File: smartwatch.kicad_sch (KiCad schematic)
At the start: 48 parts, among them IC1 LTC4413EDD-1#PBF, IC2 MIA-M10Q-00B, J3 5022441530, J5 Conn_01x04_Socket, U1 NRF52832-QFAA-R, U10 AP2127K-1.8, U2 AP2112K-3.3TRG1, U3 MAX30102, U6 ESP-PSRAM64, U7 MCP73831-2-OT, U8 W25Q128JVS, U9 LIS2DE12, X1 CX2016DB32000D0WZRC1, X2 9HT10-32.768KBZC-T

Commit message: pcb layout almost complete
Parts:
- removed C10: C, Capacitor_SMD:C_0402_1005Metric, symbol Device:C
- C9: value C -> 0.8pF
- L1: value L -> 3.9nH; footprint Inductor_SMD:L_0603_1608Metric -> Inductor_SMD:L_0402_1005Metric
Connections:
- net AC_INT: now also U1.39 (P0.27)
- net AC_SCL: now also U1.38 (P0.26)
- net AC_SDA: now also U1.37 (P0.25)
- net FLASH_CLK: now also U1.18 (P0.15)
- net GND: no longer C9.2, U1.31 (VSS1)
- net GPS_IO: now also U1.4 (P0.02)
- net GPS_RX: now also U1.5 (P0.03)
- net GPS_TX: now also U1.6 (P0.04)
- net SD_CMD: now also U1.15 (P0.12)
- net SD_DI: now also U1.21 (P0.18)
- net SRAM_CLK: now also U1.24 (P0.21)
- net SRAM_CMD: now also U1.19 (P0.16)
- net SRAM_CS: now also U1.16 (P0.13)
- net SRAM_SI02: now also U1.22 (P0.19)
- net SRAM_SIO3: now also U1.23 (P0.20)
- net SRAM_WP: now also U1.40 (P0.28)
- new net GNDREF: C9.2, U1.31 (VSS1)
- no-connect marks 29 -> 30
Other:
- moved on the sheet: L1

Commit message: -
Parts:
- removed R8: 3.3k, Resistor_SMD:R_0402_1005Metric, symbol Device:R
- added C10: 0.8pF, Capacitor_SMD:C_0402_1005Metric, symbol Device:C
- added R4: 800k, Resistor_SMD:R_0402_1005Metric, symbol Device:R
- added R9: 2M, Resistor_SMD:R_0402_1005Metric, symbol Device:R
- U1: footprint NRF52832-QFAA-R:QFN40P600X600X90-49N -> NRF52832-QFAA-R:QFN-48_NOR
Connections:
- net HR_SCL is gone; now on net AC_SCL: R1.1, U3.2 (SCL)
- net HR_SDA is gone; now on net AC_SDA: R3.1, U3.3 (SDA)
- net DISPLAY_CLK: now also U1.11 (P0.09)
- net DISPLAY_CS: now also U1.10 (P0.08)
- net DISPLAY_D/C: now also U1.8 (P0.06)
- net DISPLAY_RESET: now also U1.43 (P0.31)
- net DISPLAY_SDI: now also U1.12 (P0.10)
- net FLASH_CS: now also U1.14 (P0.11)
- net GND: now also C10.2, R9.1
- net HR_INT: now also U1.39 (P0.27)
- net SD_DO: now also U1.23 (P0.20)
- net SD_WP: now also U1.24 (P0.21)
- net SRAM_CLK: now also U1.28 (P0.23); no longer U1.24 (P0.21)
- net SRAM_SIO3: now also U1.27 (P0.22); no longer U1.23 (P0.20)
- net SRAM_WP: now also U1.29 (P0.24); no longer U1.40 (P0.28)
- net TP_INT: now also U1.9 (P0.07)
- net TP_RST: now also U1.42 (P0.30)
- net TP_SCL: now also U1.20 (P0.17)
- net TP_SDA: now also U1.17 (P0.14)
- net at BT1.1 (+), C1.1, IC1.5 (INB)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: now also R4.1
- net BT_V: now reaches U1.7 (P0.05)
- net BT_V: now also R4.2, R9.2
- net at ANT1.FEED, L1.2: now also C10.1
- net AC_INT: no longer names the net of U9.12 (INT1)
- net AC_INT: no longer U1.39 (P0.27)
- no-connect marks 30 -> 31

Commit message: pcb complete
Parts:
- removed R5, R7: 3.3k, Resistor_SMD:R_0402_1005Metric, symbol Device:R
- removed U4, U5: ~, power_pad:power_pad_5mm, symbol power_pad:pad_4mm
- added J1, J2: Conn_01x01_Pin, power_pad:power_pad_5mm, symbol Connector:Conn_01x01_Pin
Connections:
- net GNDREF is gone; now on net GND: C9.2, U1.31 (VSS1)
- net Power Supply is gone; now on net +3.3V: C16.1, C20.1, C21.1, C6.1, U1.13 (VDD1), U1.36 (VDD2), U1.48 (VDD3), U2.5 (VOUT)
- net GND: now also J1.1 (Pin_1); no longer U1.32 (DEC2)
- net SWD_VCC: now also J2.1 (Pin_1)
- no-connect marks 31 -> 32

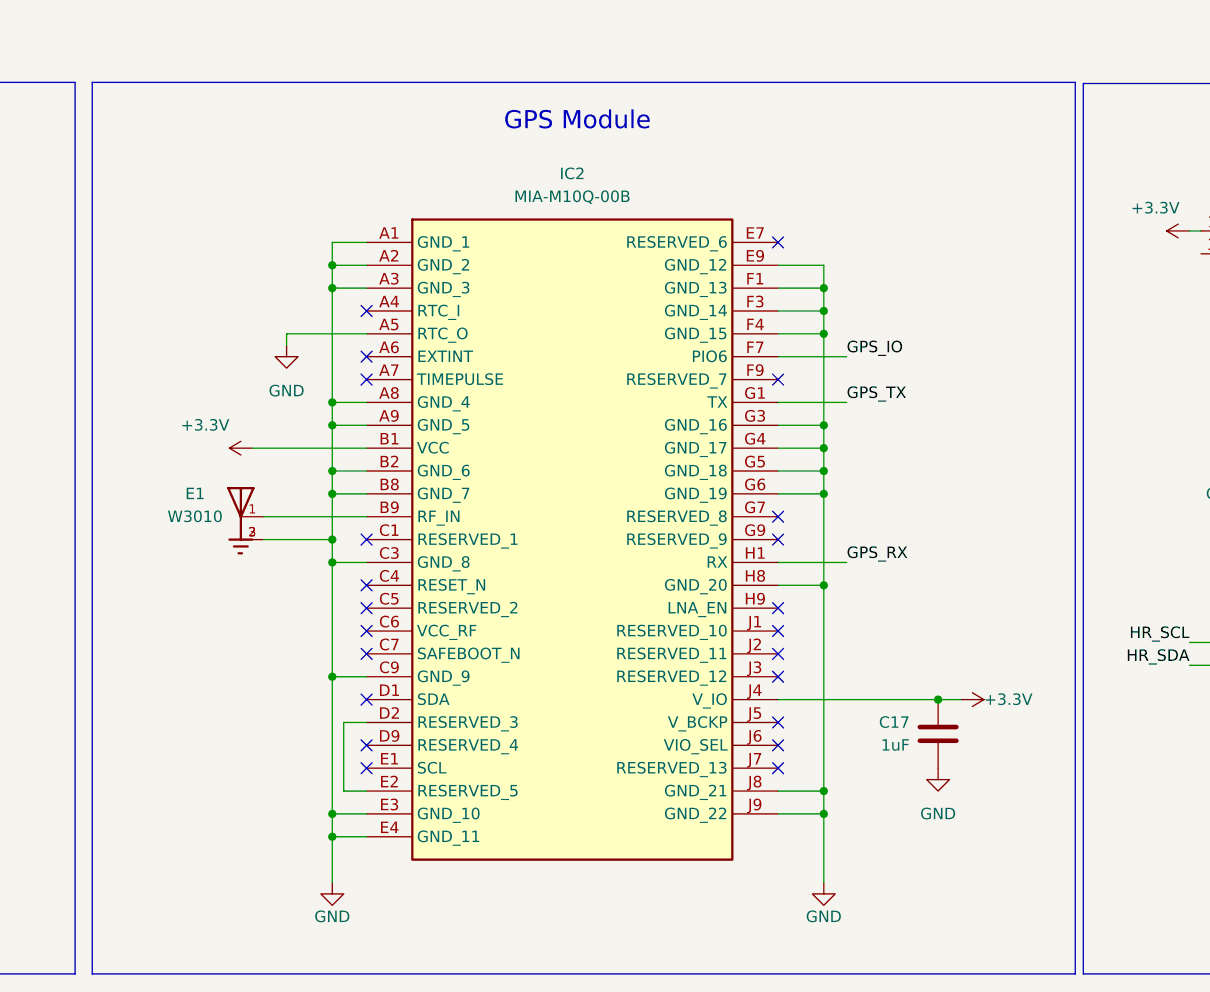
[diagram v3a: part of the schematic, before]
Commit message: changed gps module
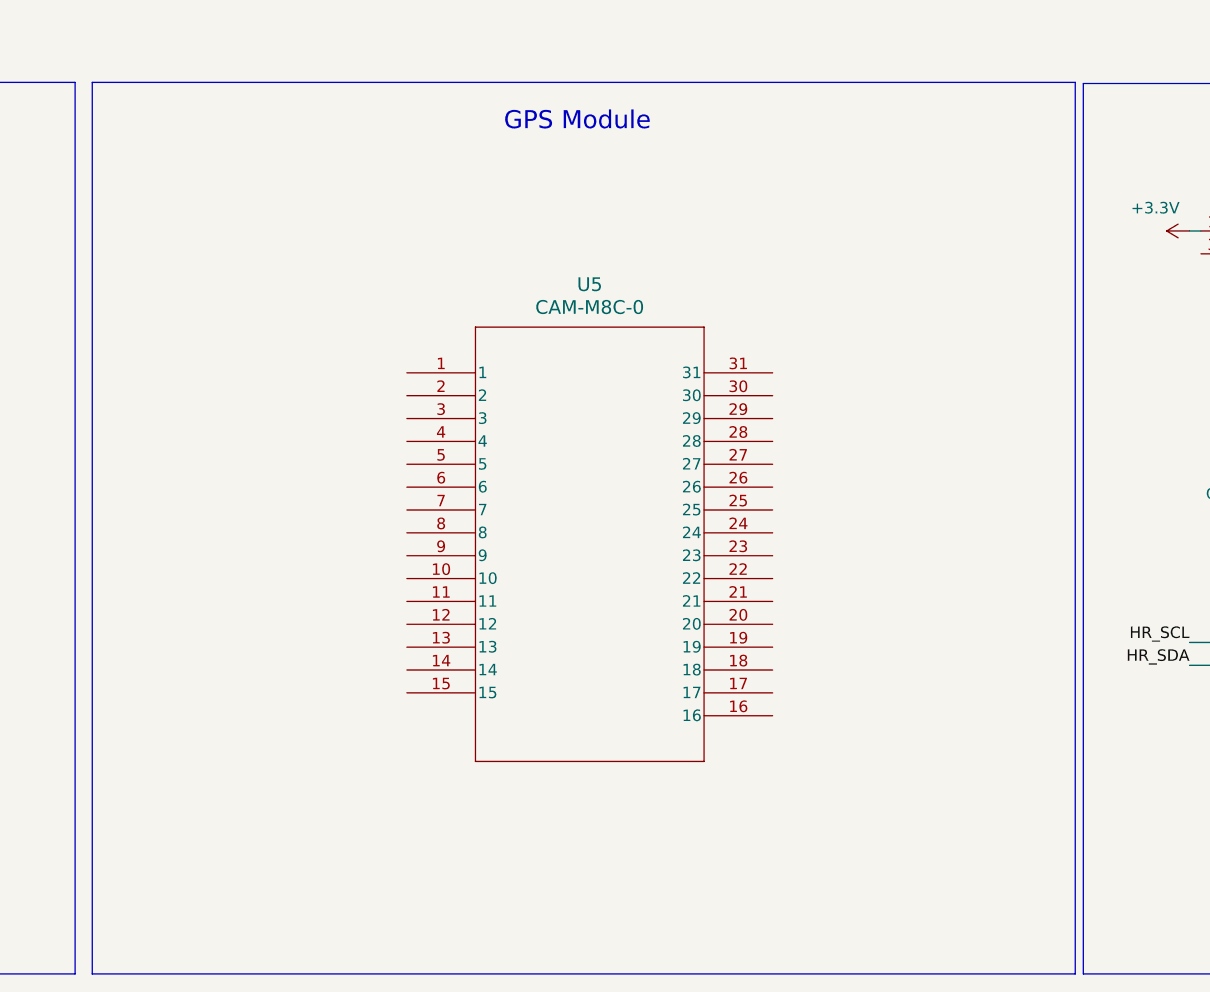
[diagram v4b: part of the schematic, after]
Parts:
- removed C17: 1uF, Capacitor_SMD:C_0402_1005Metric, symbol Device:C
- removed E1: W3010, W3010:XCVR_W3010, symbol W3010:W3010
- removed IC2: MIA-M10Q-00B, KiCad:MIAM10Q00B, symbol MIA-M10Q-00B:MIA-M10Q-00B
- added U5: CAM-M8C-0, QFN_M8C-0_UBL, symbol CAM-M8C:CAM-M8C-0
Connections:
- no-connect marks 32 -> 10

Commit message: New rtc module
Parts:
- added C17: 4.7uF, Capacitor_SMD:C_0402_1005Metric, symbol Device:C
- added J4, J6: Conn_01x01_Pin, power_pad:power_pad_4mm, symbol Connector:Conn_01x01_Pin
- added Q1: 2N7002-7-F, Package_TO_SOT_SMD:SOT-23-3, symbol Device:Q_NMOS_SGD
- added R10, R5, R7, R8: 220, symbol Device:R
- added R11: 10k, Resistor_SMD:R_0603_1608Metric, symbol Device:R
- added U4: DS1302Z+T&R, 21-0041B_8_MXM, symbol DS1302Z+T&R:DS1302Z+T&R
- added Y1: 32.768kHz, symbol Device:Crystal
- J1, J2: footprint power_pad:power_pad_5mm -> power_pad:power_pad_4mm
- R2: value 3.3k -> 22; footprint Resistor_SMD:R_0402_1005Metric -> Resistor_SMD:R_0603_1608Metric; MPN NRF52840-QIAA-R -> (none)
- R3: value 3.3k -> 10k; footprint Resistor_SMD:R_0402_1005Metric -> Resistor_SMD:R_0603_1608Metric; MPN NRF52840-QIAA-R -> (none)
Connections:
- net +3.3V: now also R2.1, U5.1, U5.8, U5.9, C17.1; no longer J3.3, J3.4, R1.2, R2.2, R3.2
- net AC_SCL: no longer R1.1
- net AC_SDA: no longer R3.1
- net GND: now also U5.10, U5.11, U5.12, U5.13, U5.14, U5.15, U5.18, U5.19, U5.21, U5.22, U5.27, U5.31, U5.4, U5.5, C17.2, J4.1 (Pin_1), Q1.1 (S), R11.1, U4.4 (GND); no longer J3.2
- net GPS_RX: now also R7.2; no longer U1.5 (P0.03)
- net GPS_TX: now also R5.2; no longer U1.6 (P0.04)
- net HR_INT: no longer R2.1
- net at U5.16: now also U5.17
- net at U5.23: now also R8.1
- net at U5.25: now also R7.1
- net at U5.26: now also R5.1
- net at U5.7: now also R10.2
- net GPS_IO: no longer names the net of U1.4 (P0.02)
- net SWD_VCC renamed VBUS
- net VBUS: now also J6.1 (Pin_1), U4.1 (VCC2), U4.8 (VCC1)
- new net: Q1.2 (G), R11.2, R3.1
- new net: U4.2 (X1), Y1.1
- new net: U4.3 (X2), Y1.2
- new net: J3.3, R2.2
- new net BACKLIGHT_EN: R3.2
- new net GPS_EXTINT: R10.1
- new net GPS_RESET: R8.2
- new net LEDK: J3.2, Q1.3 (D)
- new net RTX_CE: U4.5 (CE)
- new net RTX_IO: U4.6 (I/O)
- new net RTX_SCLK: U4.7 (SCLK)
- no-connect marks 10 -> 18
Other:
- note added: "FLASH & RAM"
- note added: "RTC"
- note removed: "External FLASH and RAM"
- moved on the sheet: ANT1, C10, C11, C12, C13, C14, C15, C16, C18, C19, C20, C21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

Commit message: changed to nrf5340 & did some rework to charging circuit
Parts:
- removed ANT1: W3008, W3008:ANTENNA_W3008, symbol W3008:W3008
- removed C11, C16, C21: 100nF, Capacitor_SMD:C_0402_1005Metric, symbol Device:C
- removed C14, C15: 12pF, Capacitor_SMD:C_0402_1005Metric, symbol Device:C
- removed C18: 100pF, Capacitor_SMD:C_0402_1005Metric, symbol Device:C
- removed C19: 1uF, Capacitor_SMD:C_0402_1005Metric, symbol Device:C
- removed C20: 4.7uF, Capacitor_SMD:C_0402_1005Metric, symbol Device:C
- removed IC1: LTC4413EDD-1#PBF, LTC4413EDD_PBF:SON50P300X300X80-11N, symbol LTC4413EDD-PBF:LTC4413EDD-1#PBF
- removed J4, J6: Conn_01x01_Pin, power_pad:power_pad_4mm, symbol Connector:Conn_01x01_Pin
- removed J5: Conn_01x04_Socket, Connector_PinHeader_2.54mm:PinHeader_1x04_P2.54mm_Vertical, symbol Connector:Conn_01x04_Socket
- removed L1: 3.9nH, Inductor_SMD:L_0402_1005Metric, symbol Device:L
- removed R4: 800k, Resistor_SMD:R_0402_1005Metric, symbol Device:R
- removed R9: 2M, Resistor_SMD:R_0402_1005Metric, symbol Device:R
- removed U1: NRF52832-QFAA-R, NRF52832-QFAA-R:QFN-48_NOR, symbol NRF52832-QFAA-R:NRF52832-QFAA-R
- removed U6: ESP-PSRAM64, Package_SO:SOIC-8_3.9x4.9mm_P1.27mm, symbol Memory_RAM:ESP-PSRAM32
- removed X1: CX2016DB32000D0WZRC1, CX2016DB32000D0WZRC1:OSCCC200X160X45N, symbol CX2016DB32000D0WZRC1:CX2016DB32000D0WZRC1
- added D1: LED_GREEN, LED_SMD:LED_0402_1005Metric, symbol Device:LED
- added D2: D_Schottky, symbol Device:D_Schottky
- added IC2: NORA-B120-00B, NORAB12000B, symbol NORA-B120-00B:NORA-B120-00B
- added J5: Conn_01x06_Pin, Connector_PinHeader_2.54mm:PinHeader_1x06_P2.54mm_Vertical, symbol Connector:Conn_01x06_Pin
- added Q2: Q_PMOS_DGS, symbol Device:Q_PMOS_DGS
- added R12: 470, Resistor_SMD:R_0402_1005Metric, symbol Device:R
- added R13: 3.3k, Resistor_SMD:R_0402_1005Metric, symbol Device:R
- added R14: 10k, symbol Device:R
- added U1: MAX17048G+T10, 21-0168E_T822-3_MXM, symbol MAX17048G_T10:MAX17048G+T10
- C10, C9: value 0.8pF -> 100uF
- C6: value 1uF -> 100uF
- R10, R5, R7, R8: footprint (none) -> Resistor_SMD:R_0402_1005Metric
- R6: value 5k -> 5.1k
- Y1: footprint (none) -> Crystal:Crystal_SMD_TXC_7M-4Pin_3.2x2.5mm
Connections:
- net ANT is gone; now on an unnamed net: C9.1
- net +3.3V: now also R1.2, R13.2; no longer C17.1, C4.1, C5.1, C6.1, R2.1, U10.1 (VIN), U2.5 (VOUT), U3.10 (VLED+), U3.9 (VLED+), U5.1, U5.8, U5.9, U9.10 (Vdd_IO), U9.2 (~{CS}), U9.9 (Vdd)
- net AC_SCL: now also R13.1
- net AC_SDA: now also R1.1
- net GND: now also J5.6 (Pin_6), R14.2
- net VBUS: now also J5.1 (Pin_1); no longer C2.1, J2.1 (Pin_1), U7.4 (V_{DD})
- net at U2.1 (VIN), U2.3 (EN): now also D2.1 (K), Q2.1 (D)
- net at C3.2, X2.1: now also IC2.C6 (P0.00/XL1)
- net at C13.2, X2.2: now also IC2.B6 (P0.01/XL2)
- net at BT1.1 (+), C1.1, U7.3 (V_{BAT}): now also Q2.3 (S)
- net VSYS: now reaches C10.1
- net VSYS: now also C17.1, C4.1, C5.1, C6.1, R2.1, U10.1 (VIN), U2.5 (VOUT), U3.10 (VLED+), U3.9 (VLED+), U5.1, U5.8, U5.9, U9.10 (Vdd_IO), U9.2 (~{CS}), U9.9 (Vdd), IC2.A7 (VDD_1), IC2.A8 (VDDH), IC2.B7 (VDD_2)
- net at U7.1 (STAT): now also D1.1 (K)
- net RTX_CE renamed RTC_CE
- net RTX_IO renamed RTC_IO
- net RTX_SCLK renamed RTC_SCLK
- new net: C2.1, D2.2 (A), J2.1 (Pin_1), Q2.2 (G), R12.1, R14.1, U7.4 (V_{DD})
- new net: D1.2 (A), R12.2
- new net RESET_N: IC2.J3 (RESET_N), J5.5 (Pin_5)
- new net SWDCLK: IC2.J2 (SWDCLK), J5.3 (Pin_3)
- new net SWDIO: IC2.H2 (SWDIO), J5.2 (Pin_2)
- new net SWO: IC2.B3 (P0.11/TRACEDATA0/SWO/CSN), J5.4 (Pin_4)
- no-connect marks 18 -> 12
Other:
- note added: "FLASH"
- note removed: "FLASH & RAM"
- moved on the sheet: BT1, C1, C13, C2, C3, C6, J1, J3, Q1, R1, R11, R2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

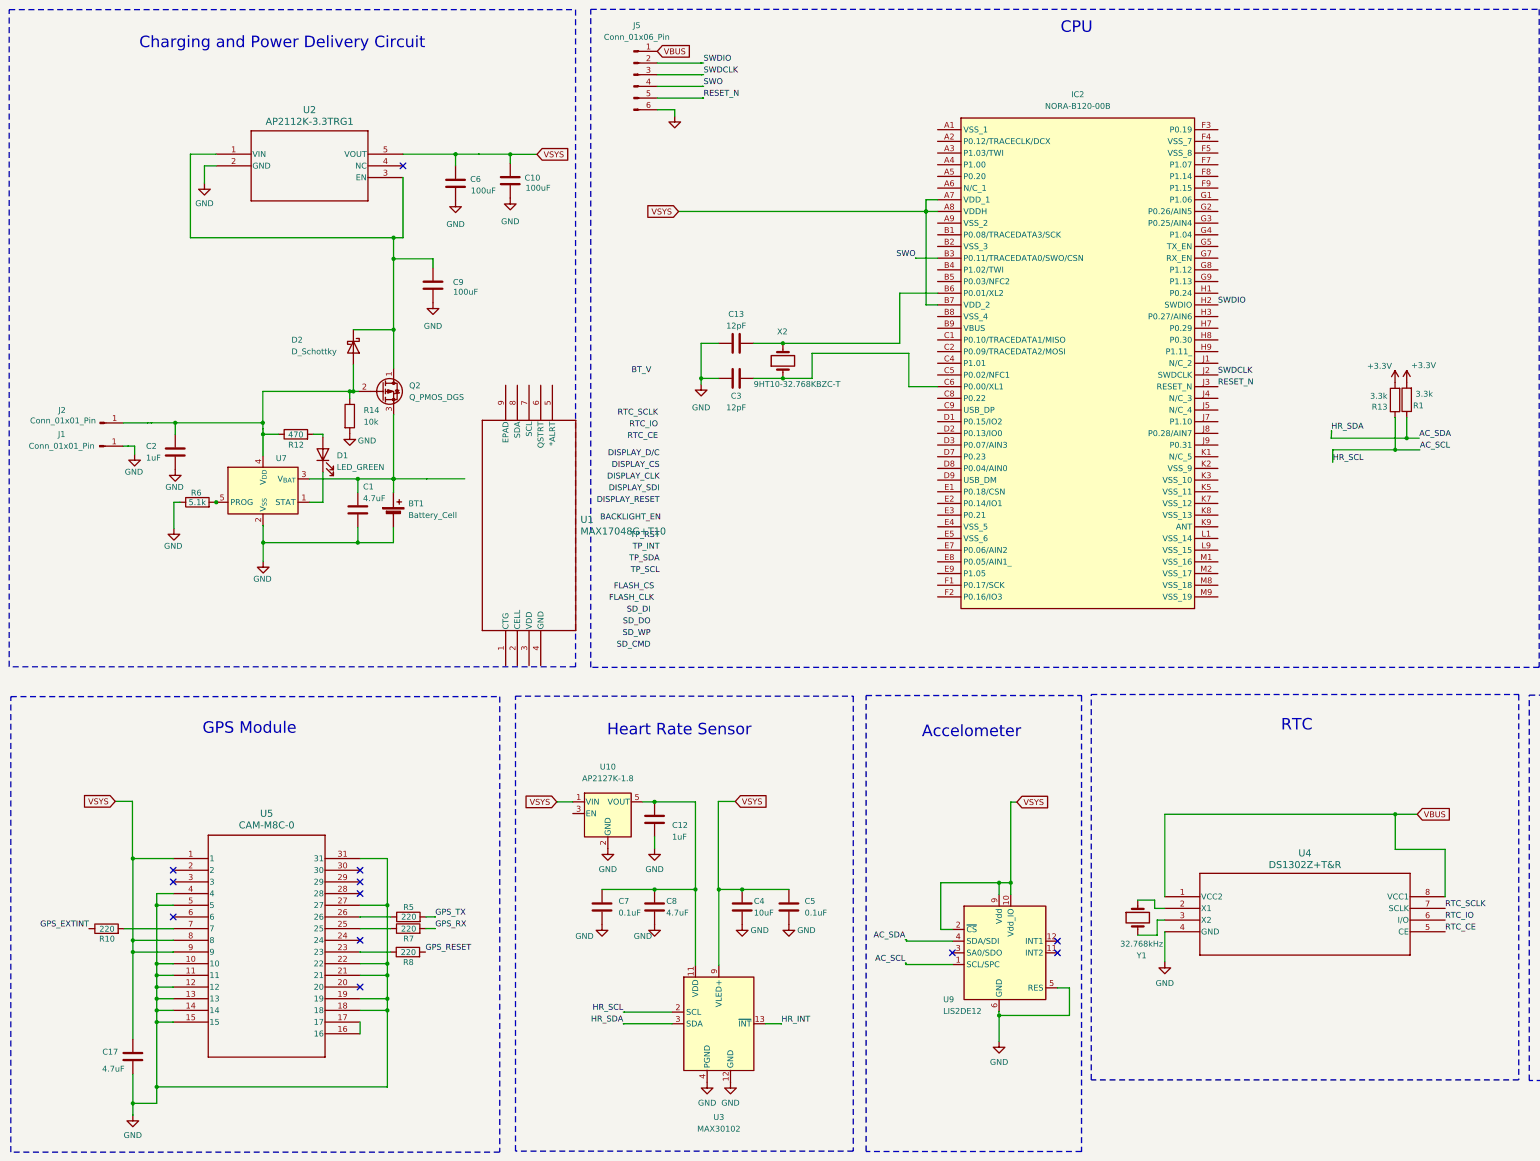
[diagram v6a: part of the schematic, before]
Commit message: added battery gauge
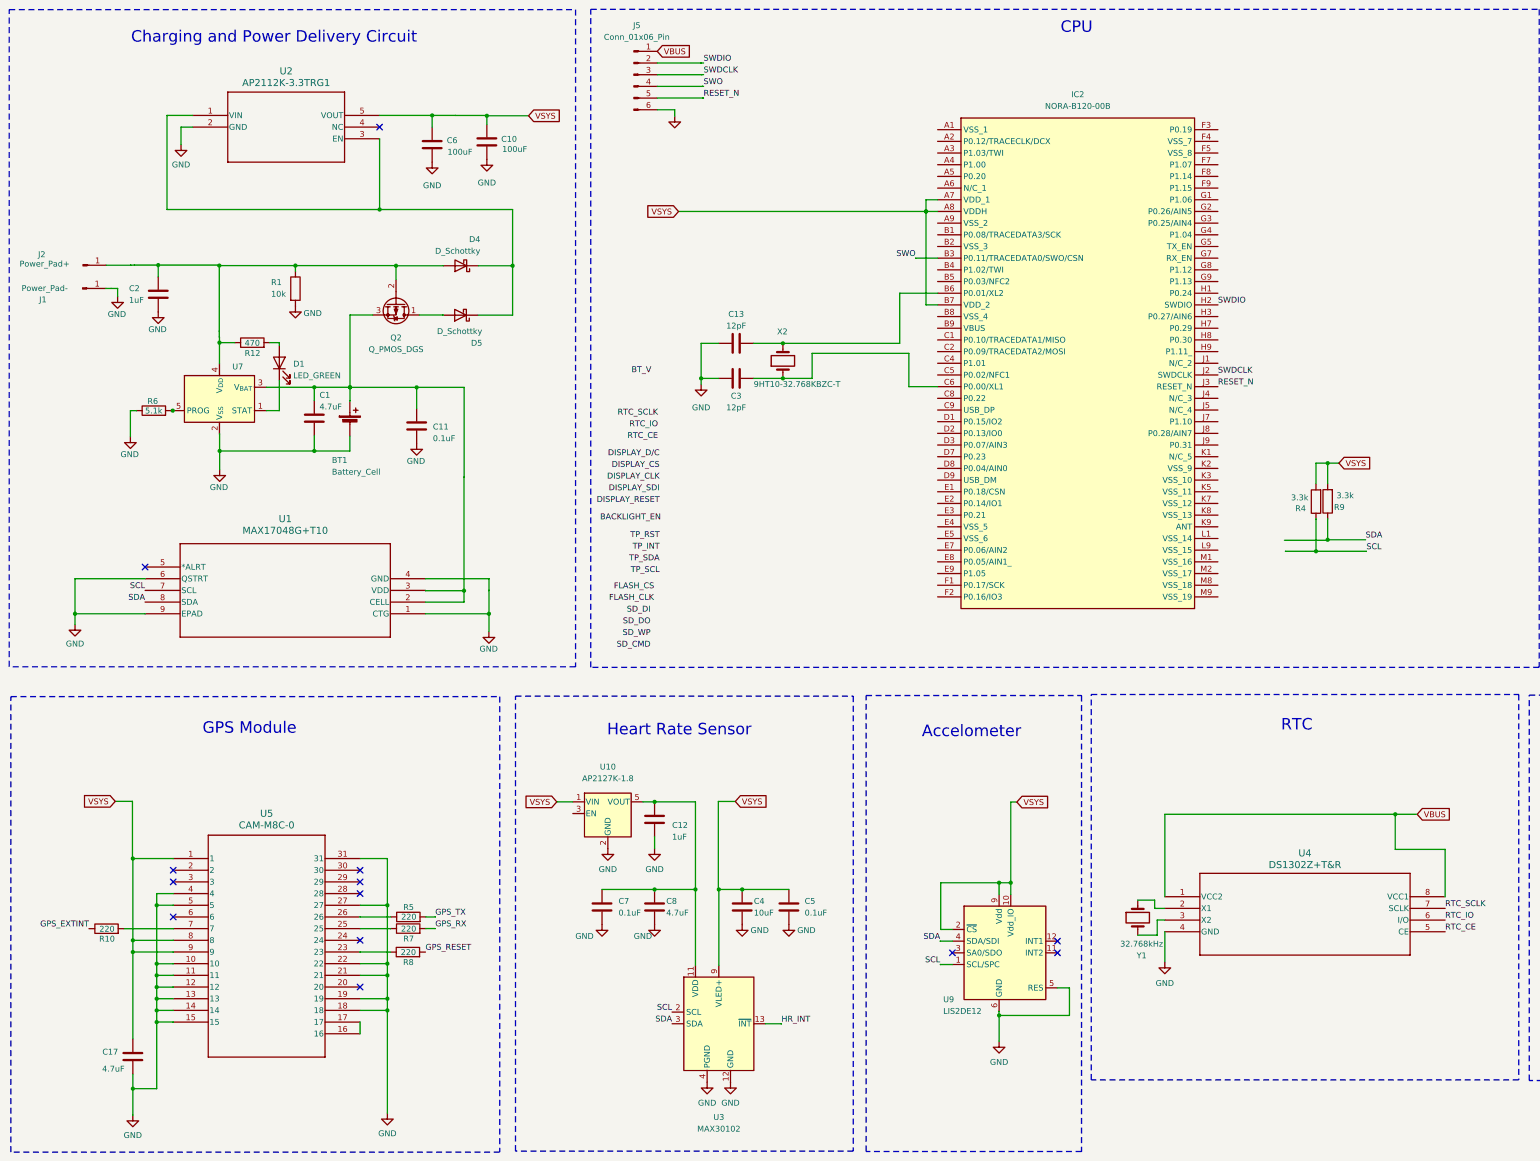
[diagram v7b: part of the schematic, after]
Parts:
- removed C9: 100uF, Capacitor_SMD:C_0402_1005Metric, symbol Device:C
- removed D2: D_Schottky, symbol Device:D_Schottky
- removed R13: 3.3k, Resistor_SMD:R_0402_1005Metric, symbol Device:R
- removed R14: 10k, symbol Device:R
- added C11: 0.1uF, Capacitor_SMD:C_0402_1005Metric, symbol Device:C
- added D4, D5: D_Schottky, symbol Device:D_Schottky
- added R4, R9: 3.3k, Resistor_SMD:R_0603_1608Metric, symbol Device:R
- J1: value Conn_01x01_Pin -> Power_Pad-
- J2: value Conn_01x01_Pin -> Power_Pad+
- R1: value 3.3k -> 10k; footprint Resistor_SMD:R_0402_1005Metric -> (none); MPN NRF52840-QIAA-R -> (none)
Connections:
- net AC_SCL is gone; now on net SCL: U3.2 (SCL), U9.1 (SCL/SPC)
- net +3.3V: no longer R1.2
- net GND: now also R1.2, U1.1 (CTG), U1.4 (GND), U1.6 (QSTRT), U1.9 (EPAD), C11.2
- net VSYS: now also R4.2, R9.2
- net at C2.1, J2.1 (Pin_1), Q2.2 (G)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: now also R1.1, D4.2 (A)
- net at U2.1 (VIN), U2.3 (EN): now also D4.1 (K), D5.1 (K); no longer Q2.1 (D)
- net at BT1.1 (+), C1.1, Q2.3 (S)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: now also U1.2 (CELL), U1.3 (VDD), C11.1
- net SCL: now reaches U1.7 (SCL)
- net SCL: now also R4.1
- net SDA: now reaches U1.8 (SDA)
- net SDA: now also U3.3 (SDA), U9.4 (SDA/SDI), R9.1
- removed net AC_SDA: R1.1, U3.3 (SDA), U9.4 (SDA/SDI)
- new net: D5.2 (A), Q2.1 (D)
- no-connect marks 12 -> 13
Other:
- moved on the sheet: BT1, C1, C10, C2, C6, D1, J1, J2, Q2, R12, R6, U1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
